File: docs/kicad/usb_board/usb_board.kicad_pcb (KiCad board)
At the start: 2 copper layers, 38 x 24 mm, 9 parts, among them J1 USB_OUT, J2 PWR_IO, J3 JUMP_OUT, J4 JUMP_IN, J5 myUSB_B_Socket

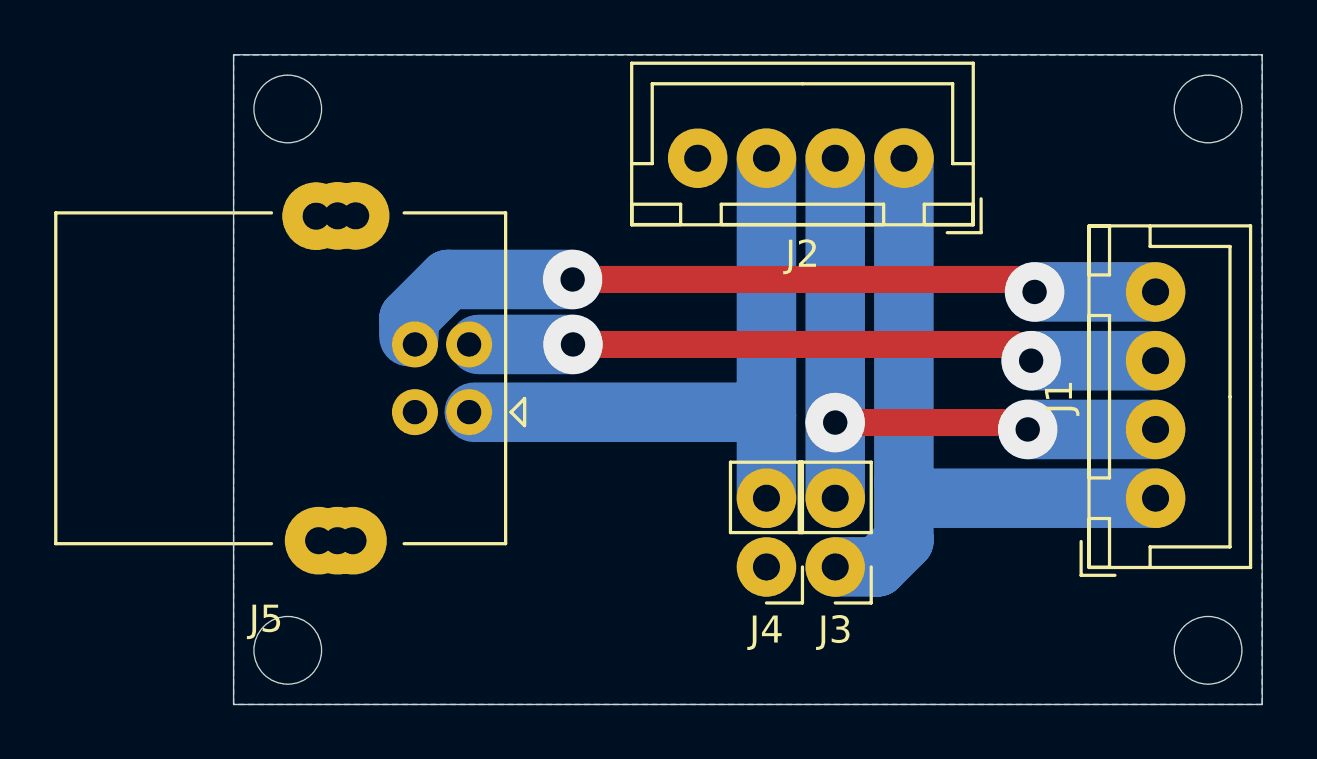
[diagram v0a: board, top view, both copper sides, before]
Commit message: REDRAW and REPRINT TeensyExpression Box (silver)
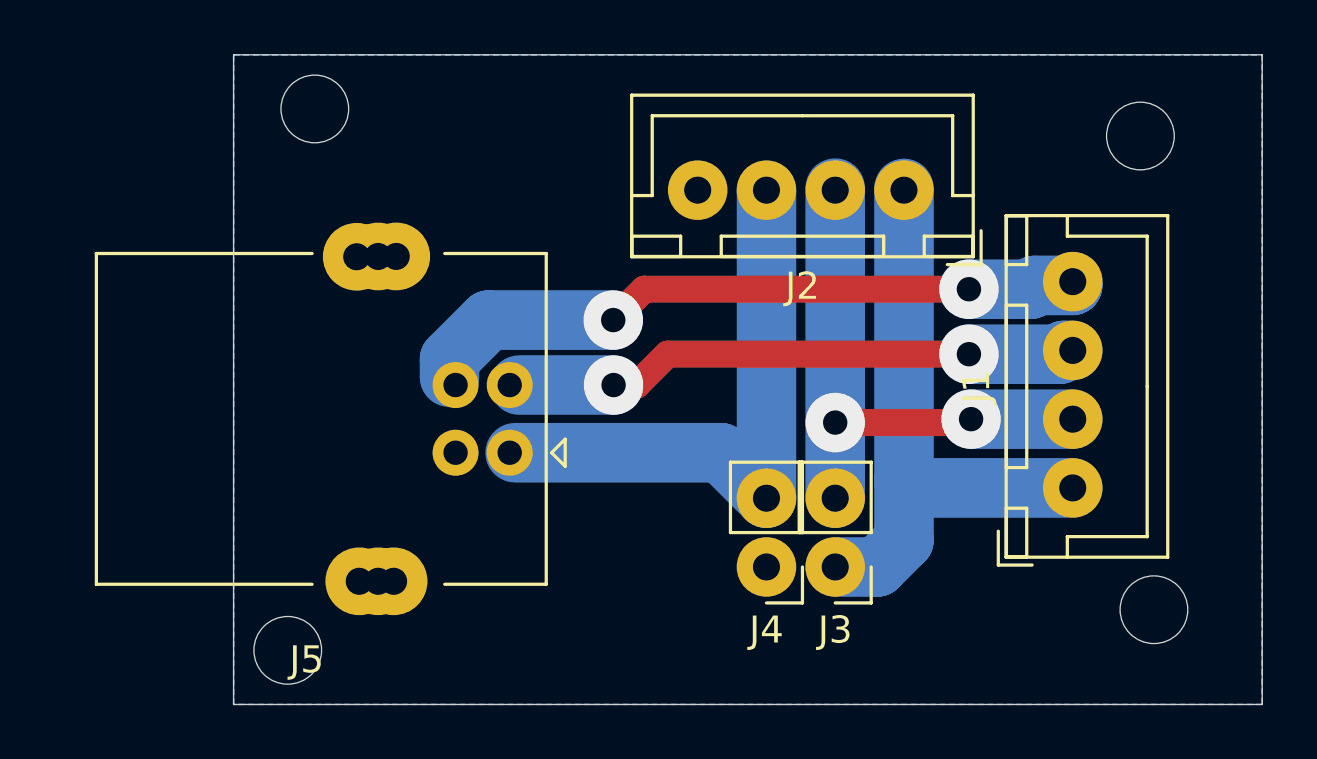
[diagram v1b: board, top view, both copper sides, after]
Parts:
- removed the REF** at (2.00, -22.0)
- removed the REF** at (36.0, -22.0)
- removed the REF** at (36.0, -2.00)
- added REF**: myMountingHole_2.5mm, 0_my_footprints:myMountingHole_2.5mm, F.Cu at (3.00, -22.0)
- added REF**: myMountingHole_2.5mm, 0_my_footprints:myMountingHole_2.5mm, F.Cu at (33.5, -21.0)
- added REF**: myMountingHole_2.5mm, 0_my_footprints:myMountingHole_2.5mm, F.Cu at (34.0, -3.50)
- moved J1 3.08 mm to (31.0, -8.00)
- moved J5 2.12 mm to (10.2, -9.30)
- moved J2 1.18 mm to (24.8, -19.0)
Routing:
- net Net-(J1-Pad1): track 26.6 -> 22.3 mm
- net D-: track 25.3 -> 21.0 mm
- net Net-(J1-Pad2): track 24.5 -> 20.3 mm
- net D+: track 29.0 -> 25.0 mm
- net +5V: track 23.0 -> 21.3 mm

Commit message: final changes for redrawn, reprinted, and rebuilt teensyExpression box (teensyExpressionRedraw.f3z)
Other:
- board text added: "yellow white red black"
